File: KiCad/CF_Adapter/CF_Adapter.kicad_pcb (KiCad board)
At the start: 2 copper layers, 38.1 x 53.3 mm, 3 parts, among them J1 Z-Fighter IDE Connector, J2 CF Card Socket

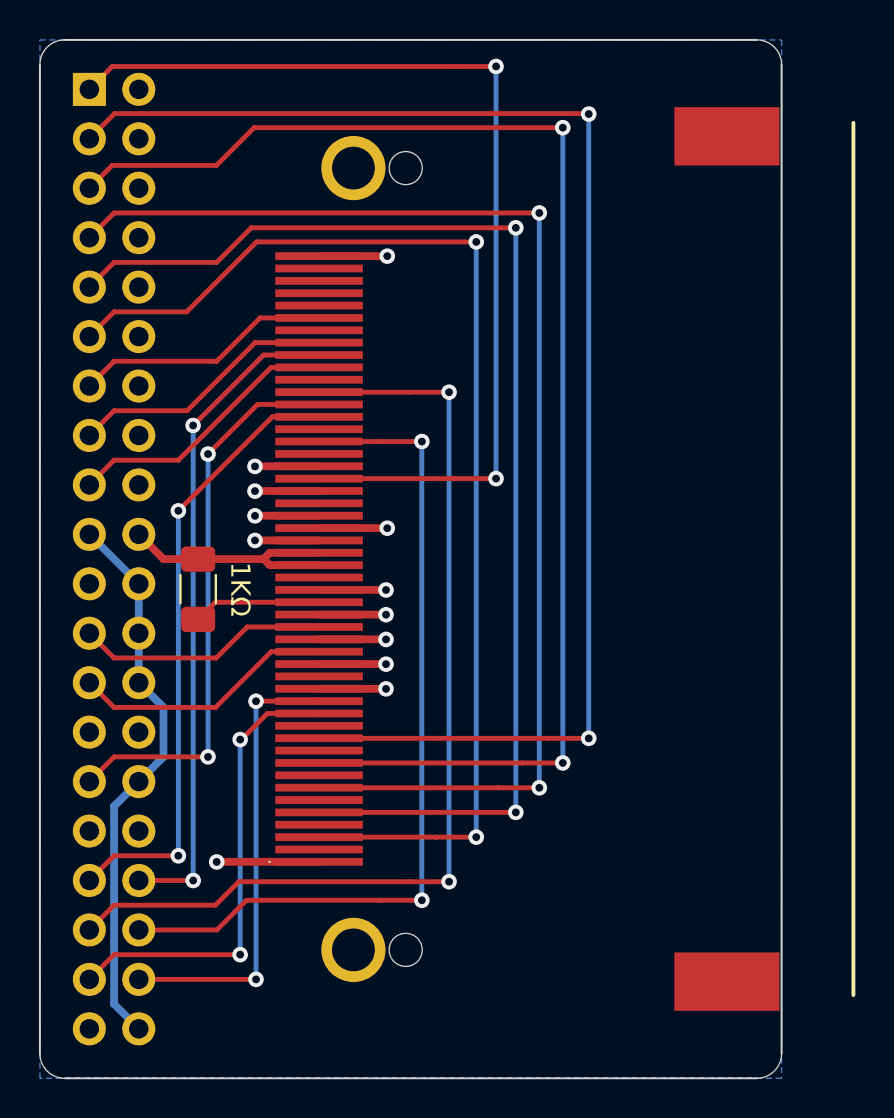
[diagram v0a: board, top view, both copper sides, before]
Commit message: Update CF_Adapter.kicad_pcb
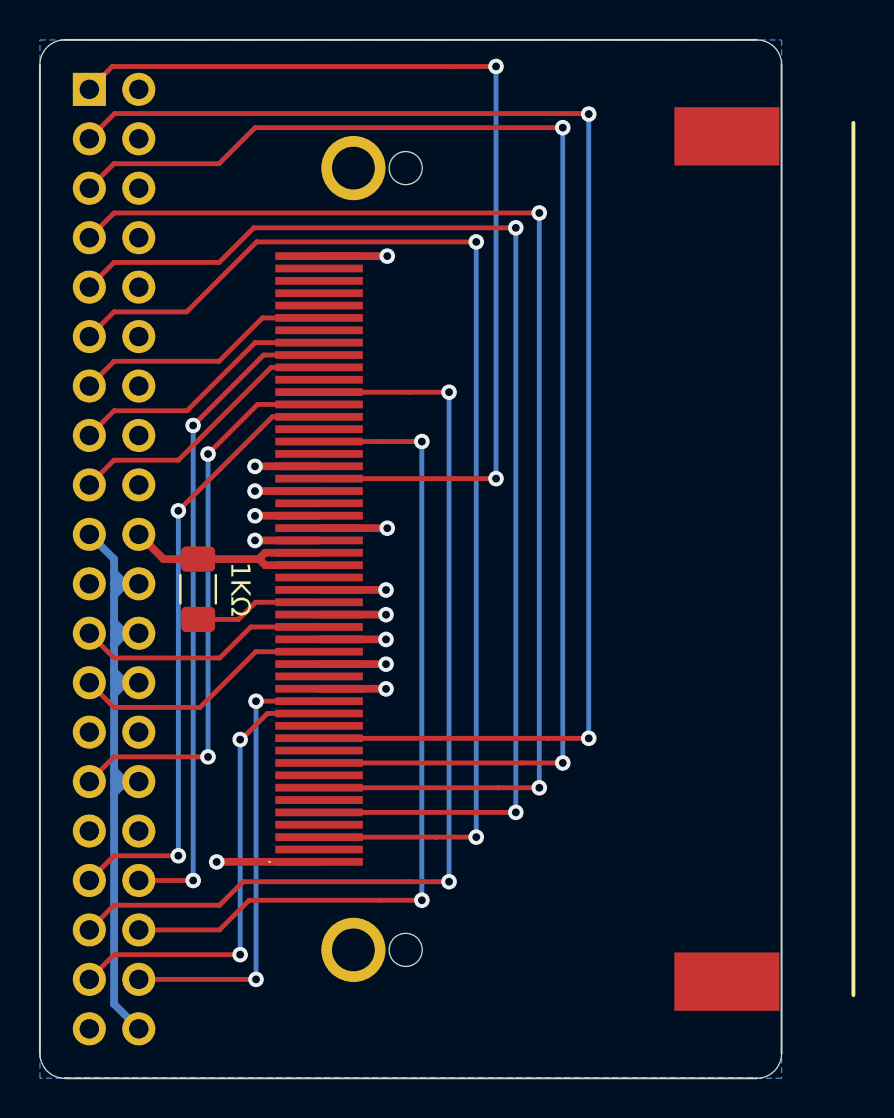
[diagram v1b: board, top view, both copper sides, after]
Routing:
- net GND: track 71.3 -> 82.2 mm
